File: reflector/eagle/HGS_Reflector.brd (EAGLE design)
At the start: 100 x 100 mm, 24 parts, among them J1 U.FL, U3 LP2985XX-N

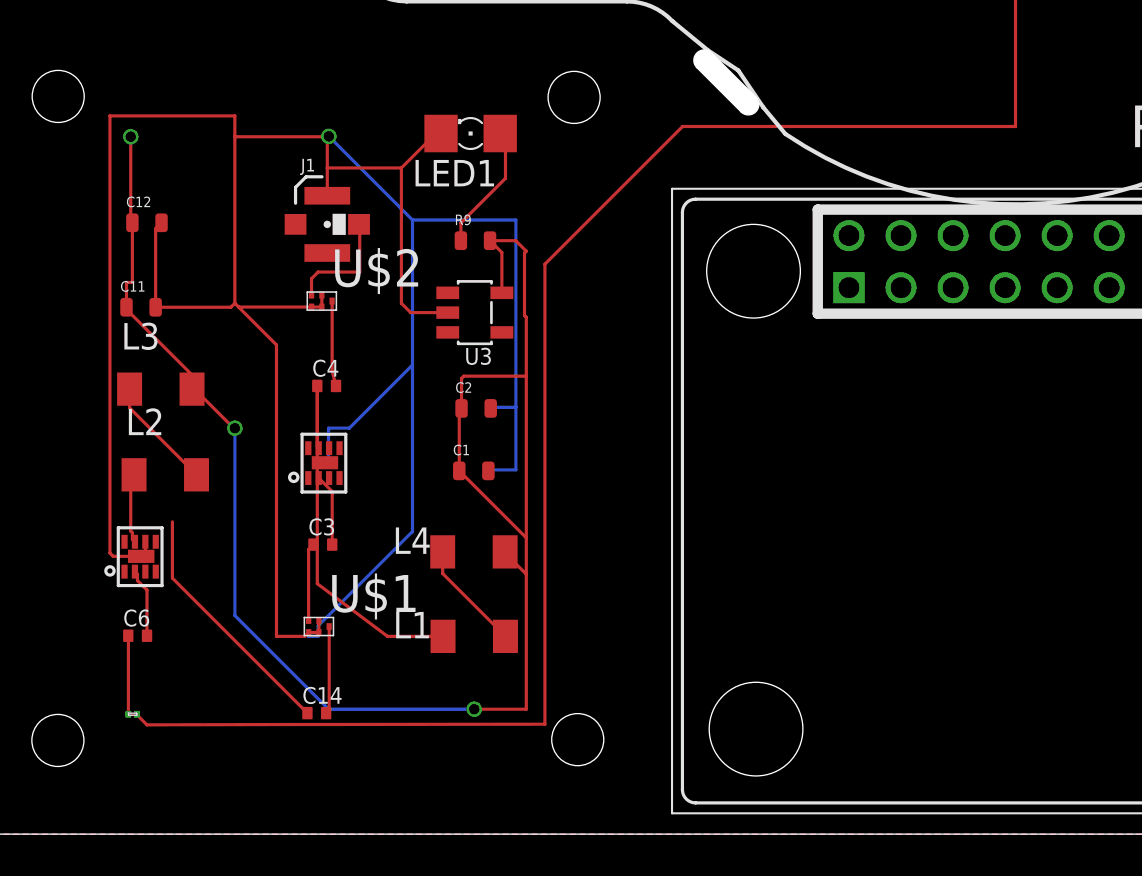
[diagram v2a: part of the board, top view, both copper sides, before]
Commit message: I incorporated the 1/4 wave transformer part (TM-QWT-2.422GHz.lbr) into the HGS reflector board, but I have not yet consulted with the person who designed the part in order to situate it properly.
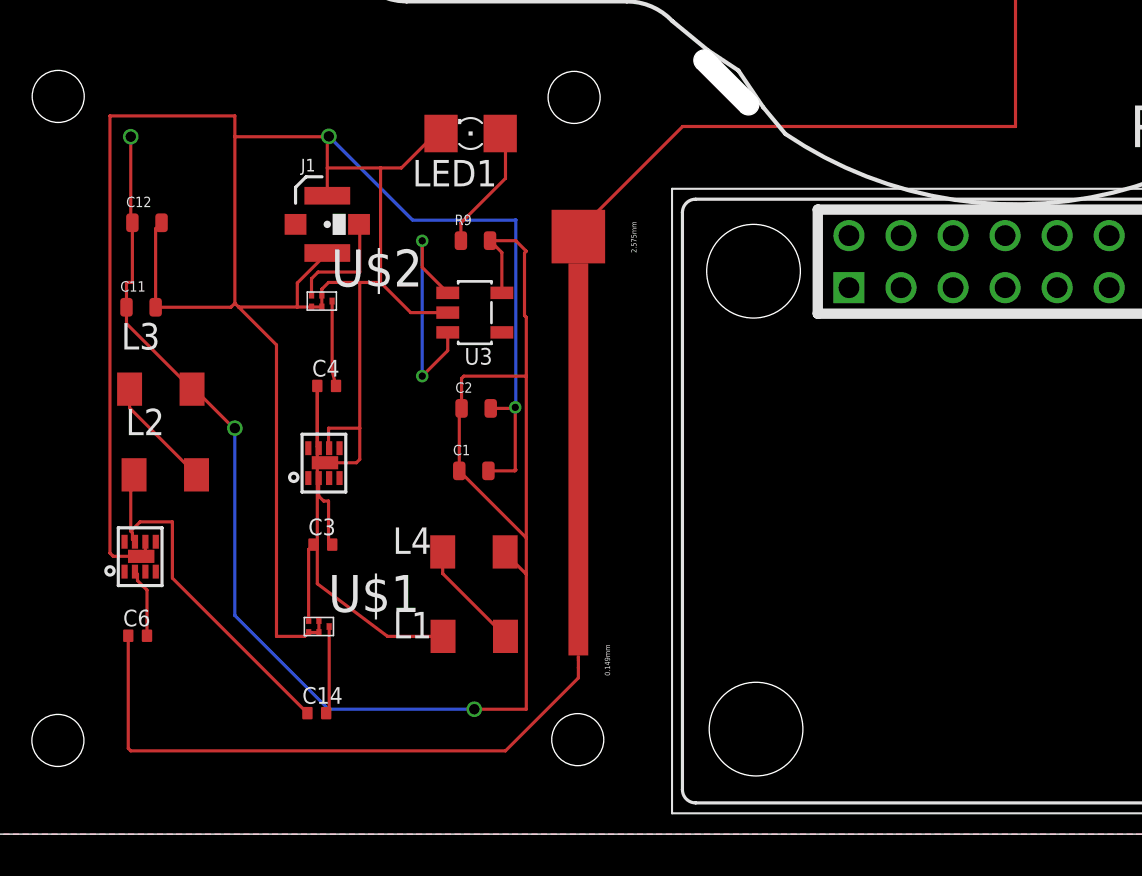
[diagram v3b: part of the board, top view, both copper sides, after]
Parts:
- U$3: value 1/4_WAVE_TRF -> QWT2.422; device HGS_Data_Parts:1/4_WAVE_TRF -> TM-QWT-2.422GHz:QWT_2.422G
- moved U$3 24.7 mm to (29.0, 18.0), turned to 270 degrees
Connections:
- net N$12: now also U$3.P$1; no longer U$3.1
- net N$9: now also U$3.P$2; no longer U$3.3
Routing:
- net N$12: track 84.7 -> 40.8 mm
- net N$9: track 3.80 -> 29.5 mm
- net 5V: track 0.00 -> 12.1 mm, vias 0 -> 2
- net GND: track 147.0 -> 137.9 mm, vias 1 -> 2
- net N$16: track 15.0 -> 18.0 mm
- net 3.3V: track 81.6 -> 82.7 mm

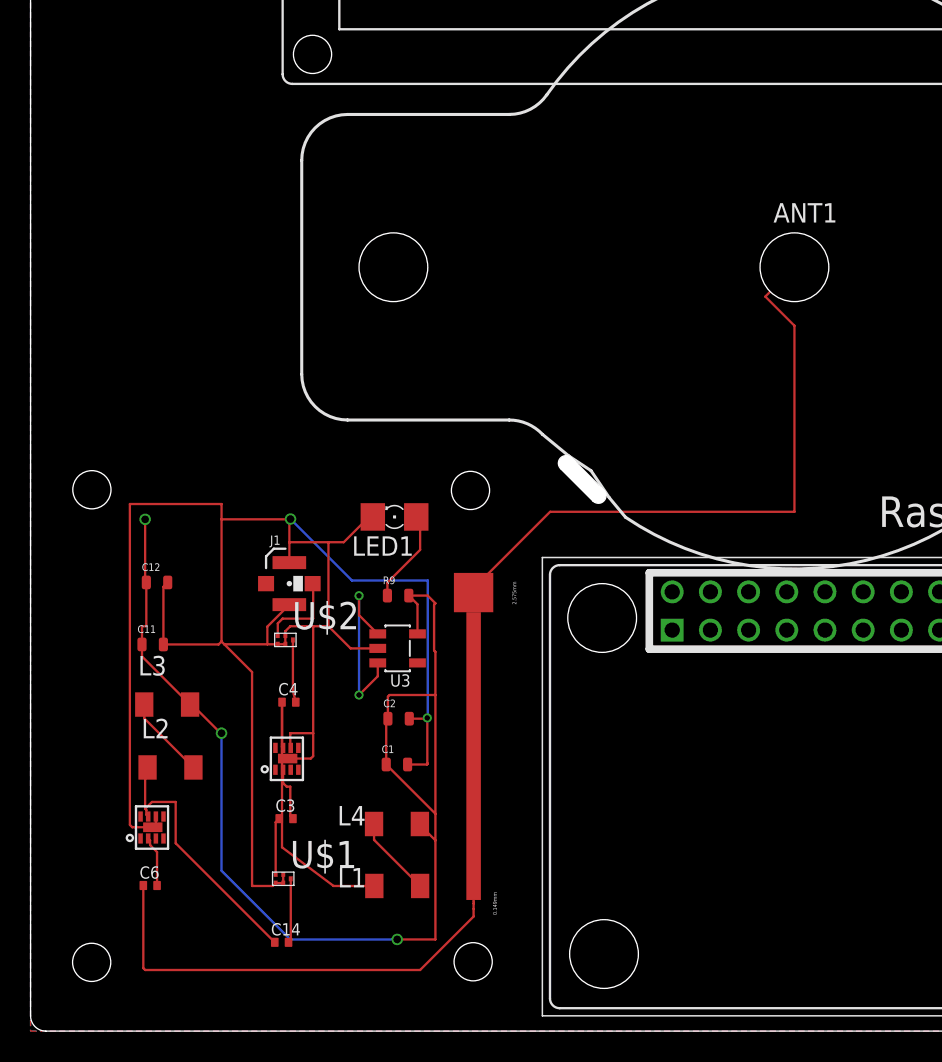
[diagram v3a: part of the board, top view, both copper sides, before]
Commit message: I started reorganizing the HGS board in order to minimize all of the trace lengths.
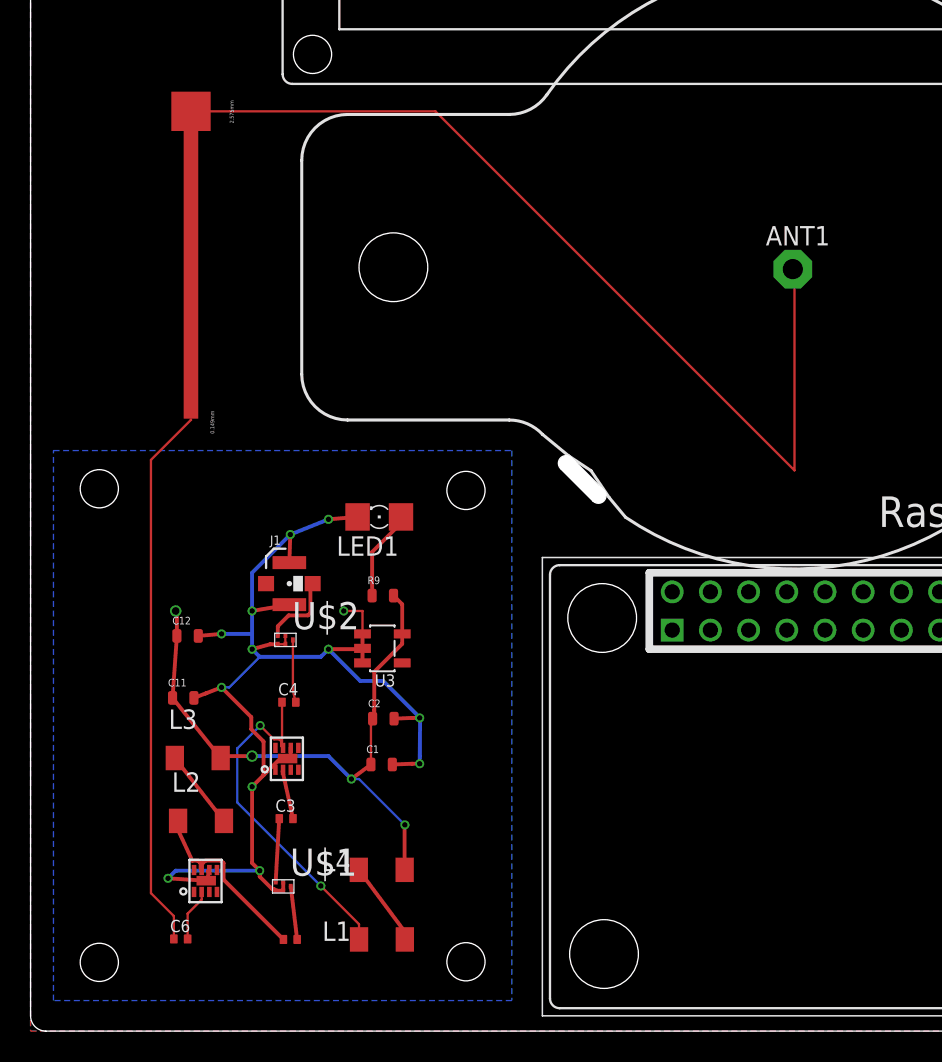
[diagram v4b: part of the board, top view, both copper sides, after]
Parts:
- moved U$3 36.5 mm to (10.5, 49.5)
- moved U$7 4.95 mm to (11.5, 9.84)
- moved C11 4.03 mm to (9.99, 21.8)
- moved C12 4.03 mm to (10.3, 25.9)
- moved L2 4.03 mm to (11.2, 13.8)
- moved L3 4.03 mm to (10.9, 17.9)
- moved C6 4.03 mm to (9.83, 6.03)
- moved L1 3.64 mm to (23.0, 6.00)
- moved L4 3.16 mm to (23.0, 10.6)
- moved C1 1.00 mm to (23.0, 17.4)
- moved C2 1.00 mm to (23.1, 20.4)
- moved LED1 1.00 mm to (22.8, 33.7)
- moved R9 1.00 mm to (23.1, 28.5)
- moved U3 1.00 mm to (23.0, 25.1)
- moved C14 0.59 mm to (17.0, 6.00)
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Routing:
- net GND: track 137.9 -> 79.9 mm, vias 2 -> 12
- net 3.3V: track 82.7 -> 41.5 mm, vias 3 -> 4
- net N$12: track 40.8 -> 62.5 mm
- net 5V: track 12.1 -> 4.62 mm, vias 2 -> 1
- net N$9: track 29.5 -> 35.7 mm
- net N$16: track 18.0 -> 12.2 mm
- net N$13: track 19.4 -> 23.1 mm, vias 0 -> 2
- net N$6: track 4.22 -> 3.50 mm
- added copper zone on layer 16, net GND

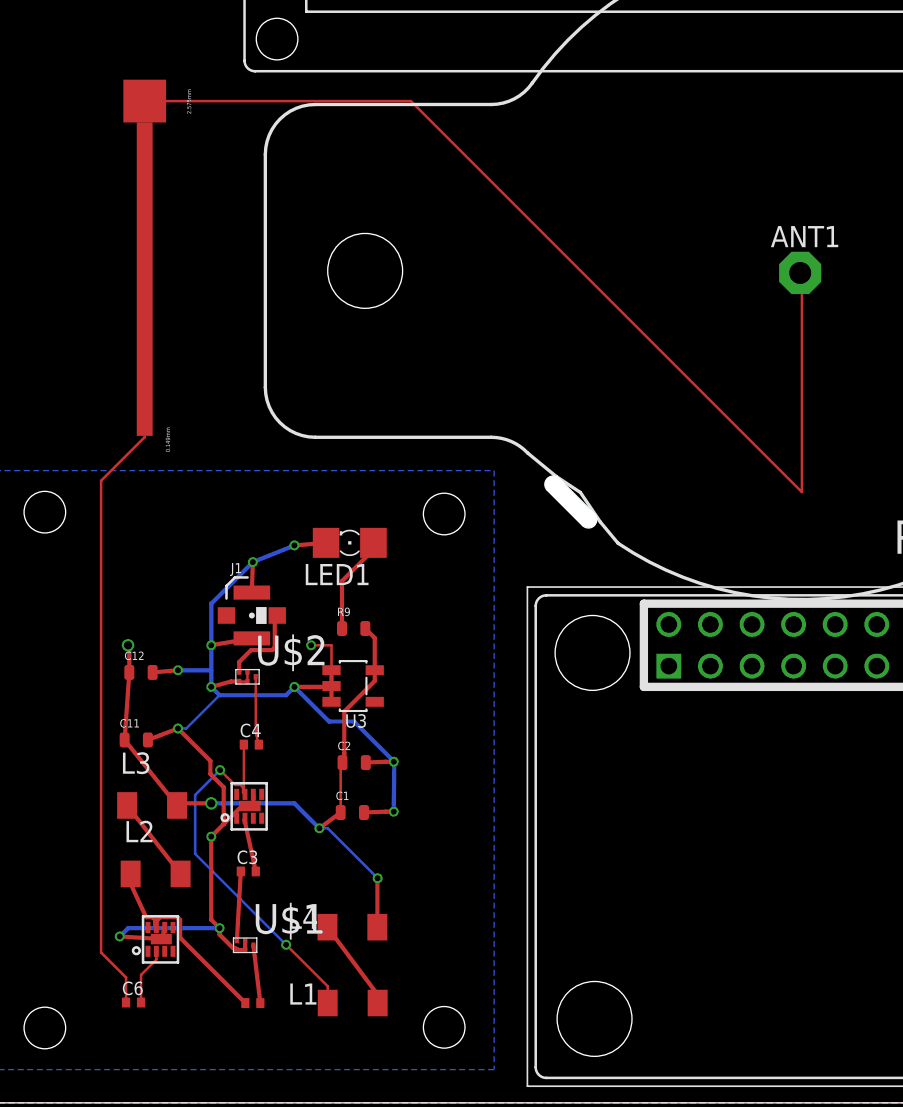
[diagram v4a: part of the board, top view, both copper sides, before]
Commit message: I continued optimizing the trace lengths for the parts on the HGS board, but have not yet been able to situation the 1/4 wave transformer part on the ground plane with the other parts.
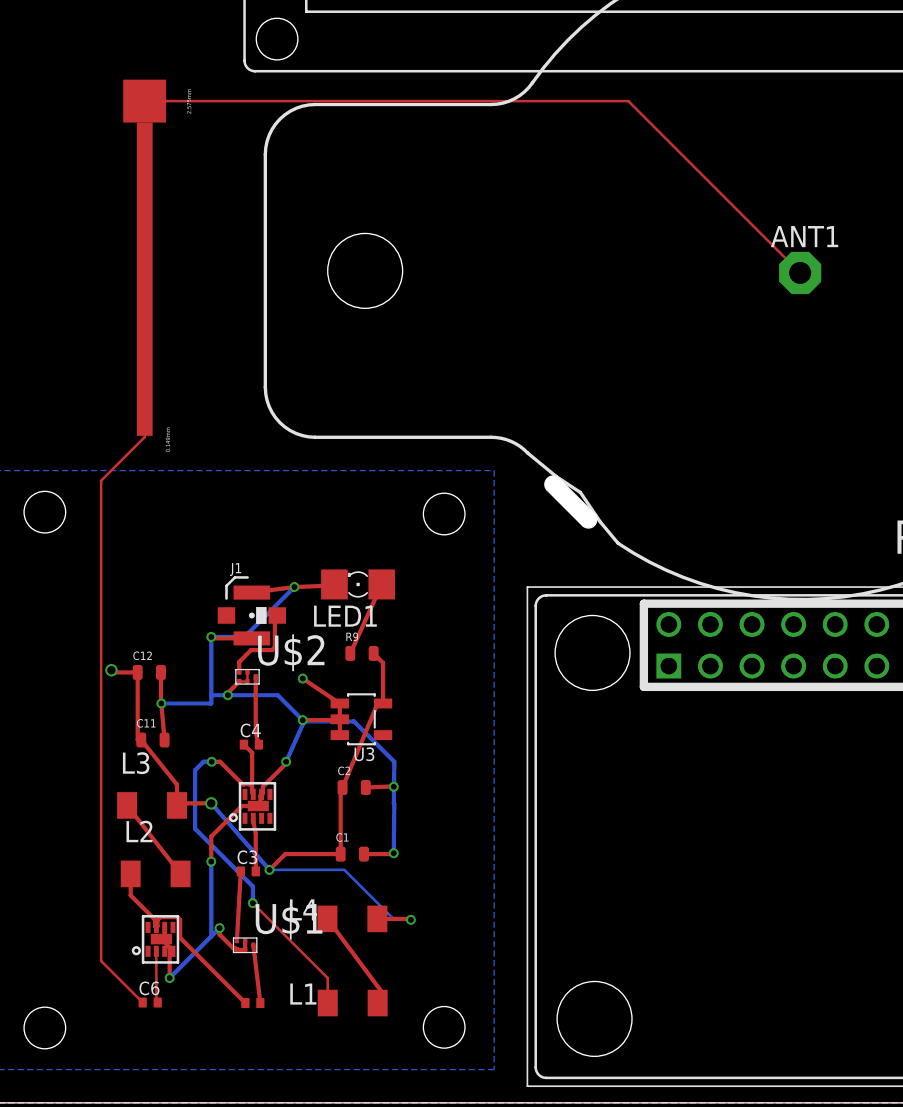
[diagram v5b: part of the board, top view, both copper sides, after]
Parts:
- moved LED1 2.55 mm to (23.3, 31.2)
- moved C1 2.50 mm to (23.0, 14.9)
- moved U3 2.06 mm to (23.5, 23.1)
- moved R9 1.58 mm to (23.6, 27.0)
- moved C2 1.50 mm to (23.1, 18.9)
- moved C11 1.00 mm to (11.0, 21.8)
- moved C6 1.00 mm to (10.8, 6.03)
- moved C12 0.50 mm to (10.8, 25.9)
- moved L4 0.50 mm to (23.0, 11.1)
- moved U$6 0.50 mm to (17.3, 17.8)
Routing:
- net N$12: track 62.5 -> 43.7 mm
- net 3.3V: track 41.5 -> 47.8 mm
- net GND: track 79.9 -> 77.3 mm, vias 12 -> 11
- net N$13: track 23.1 -> 25.1 mm
- net N$10: track 6.10 -> 4.56 mm
- net N$14: track 5.71 -> 6.37 mm

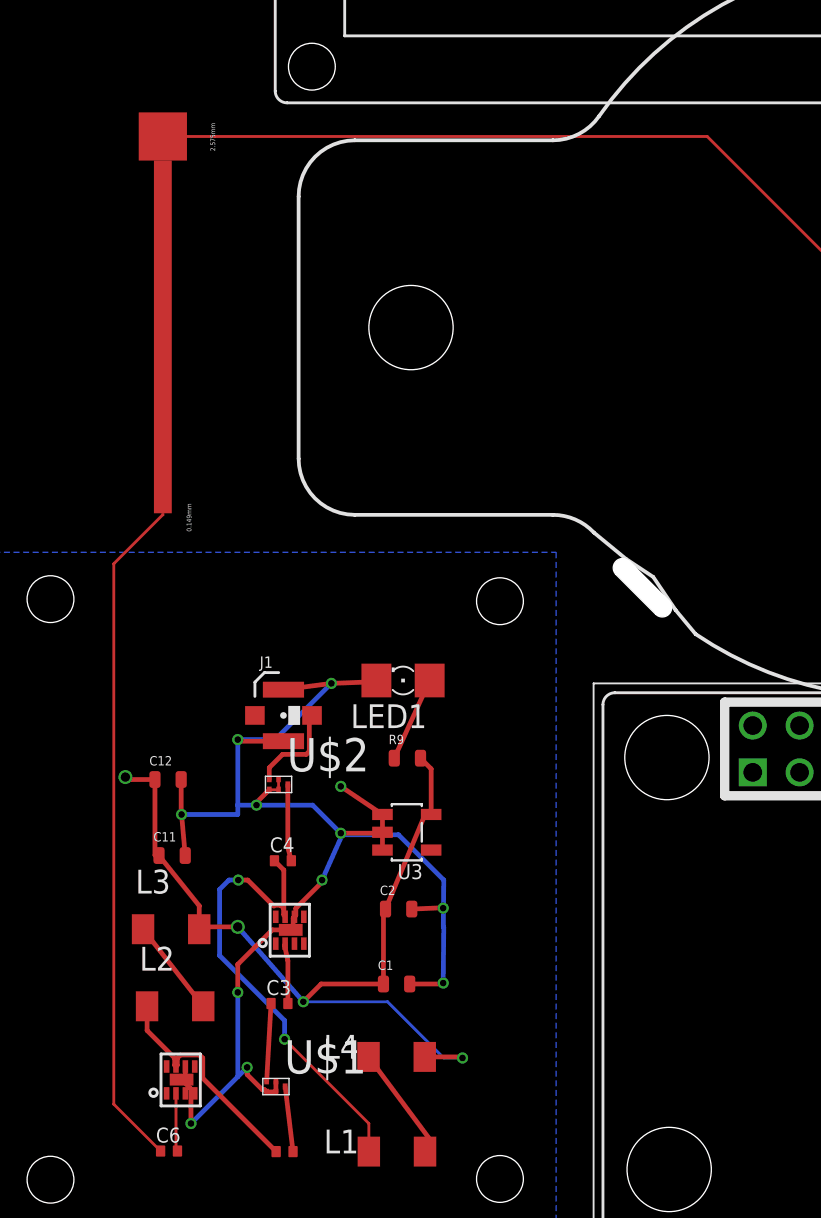
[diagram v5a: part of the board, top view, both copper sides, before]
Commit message: I made a few more wire adjustments on the HGS board.
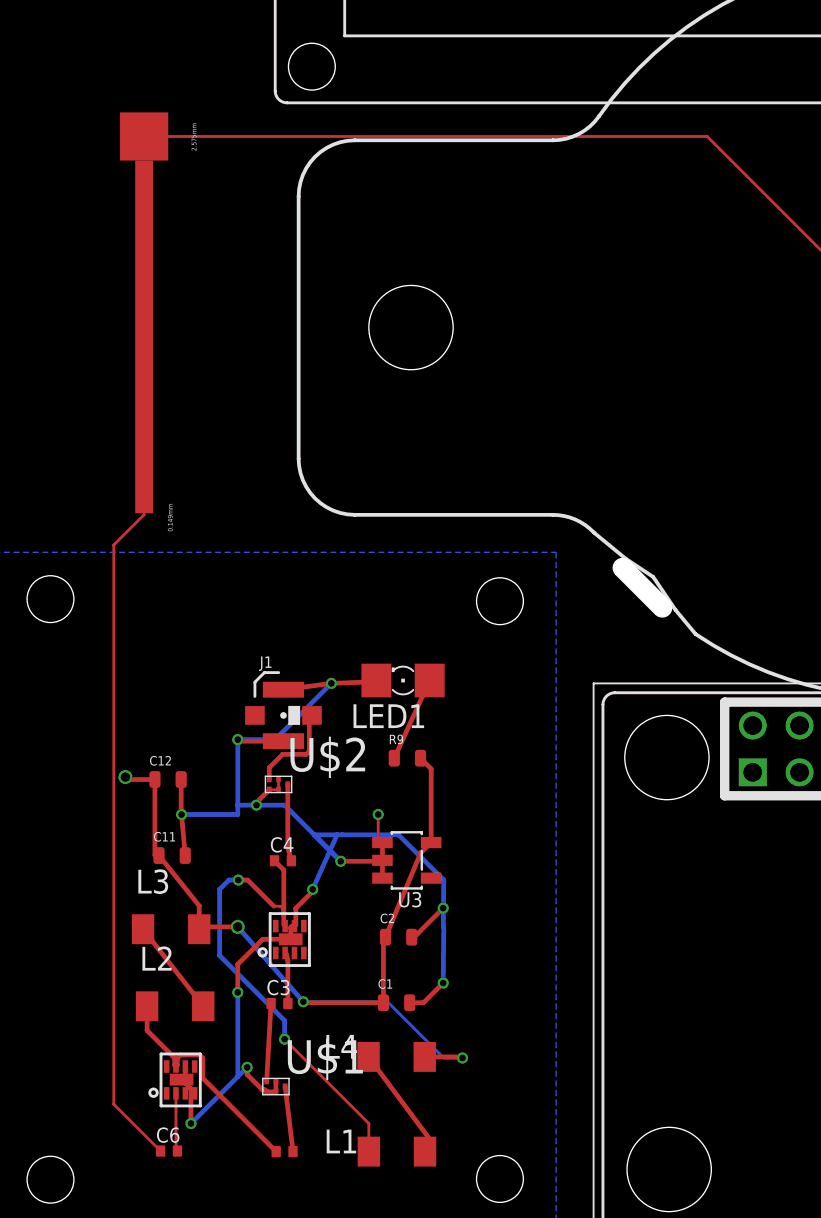
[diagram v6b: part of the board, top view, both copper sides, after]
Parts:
- moved C2 1.50 mm to (23.1, 17.4)
- moved U3 1.50 mm to (23.5, 21.6)
- moved C1 1.00 mm to (23.0, 13.9)
- moved U$3 1.00 mm to (9.50, 49.5)
- moved U$6 0.50 mm to (17.3, 17.3)
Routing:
- net GND: track 77.3 -> 82.6 mm
- net 5V: track 4.58 -> 3.49 mm
- net N$12: track 43.7 -> 44.7 mm
- net N$13: track 25.1 -> 25.6 mm
